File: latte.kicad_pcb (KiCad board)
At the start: 4 copper layers, 50 x 50 mm, 76 parts, among them J1 SOIC bite, J2 USB_C_Receptacle_USB2.0, J3 USB_C_Receptacle_USB2.0, J4 USB_C_2.0, J5 USB_A, J6 OUT1, J8 SENSE1, Q1 IRLML0030, SW1 USB BOOT, U1 RP2040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

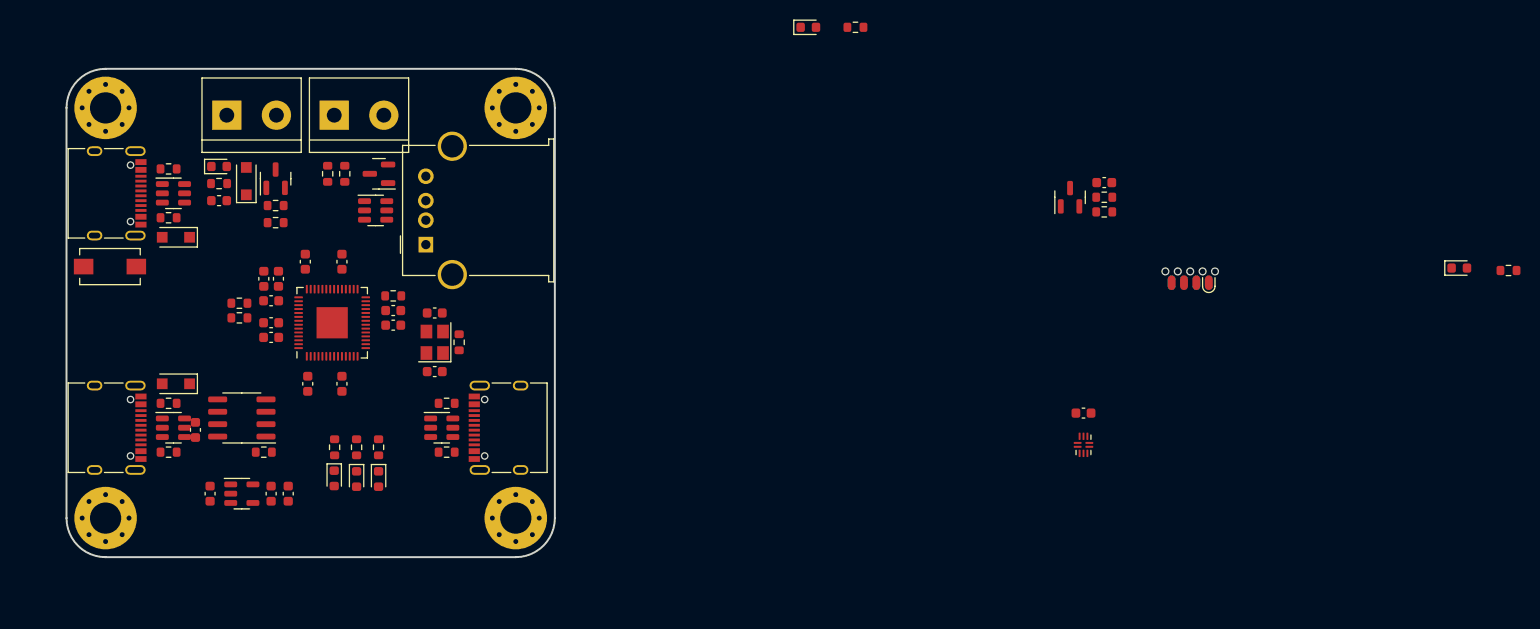
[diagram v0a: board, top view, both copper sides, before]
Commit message: Diff pair routing done
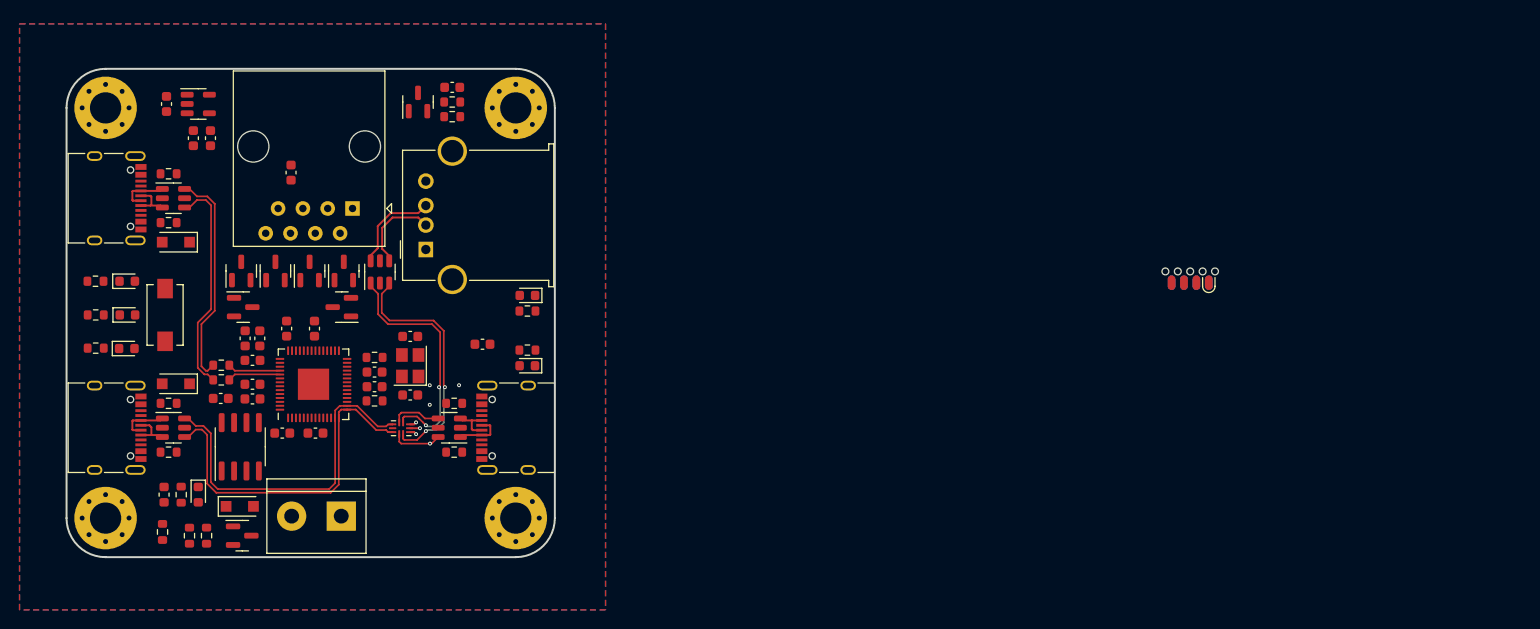
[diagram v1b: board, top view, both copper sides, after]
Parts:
- removed D13: BAV99, Package_TO_SOT_SMD:SOT-23
- removed J8: SENSE1, TerminalBlock:TerminalBlock_bornier-2_P5.08mm
- removed R27: 10k, Resistor_SMD:R_0603_1608Metric
- removed R29: DNP, Resistor_SMD:R_0603_1608Metric
- added C20: 100n, Capacitor_SMD:C_0603_1608Metric, F.Cu at (135.2, 81.6)
- added D11: BAV99, Package_TO_SOT_SMD:SOT-23, F.Cu at (133.6, 91.7)
- added D12: BAV99, Package_TO_SOT_SMD:SOT-23, F.Cu at (130.1, 91.7)
- added D15: BAV99, Package_TO_SOT_SMD:SOT-23, F.Cu at (137.1, 91.7)
- added D16: BAV99, Package_TO_SOT_SMD:SOT-23, F.Cu at (140.4, 95.4)
- added D17: BAV99, Package_TO_SOT_SMD:SOT-23, F.Cu at (140.6, 91.7)
- added D4: BAV99, Package_TO_SOT_SMD:SOT-23, F.Cu at (130.3, 95.4)
- added J7: SMART PROBE, Connector_RJ:RJ45_Amphenol_54602-x08_Horizontal, F.Cu at (141.5, 85.3)
- moved R16 100.8 mm to (159.4, 99.8), turned to 180 degrees
- moved D6 95.9 mm to (159.4, 101.4), turned to 180 degrees
- moved U6 69.9 mm to (146.5, 107.8), turned to -90 degrees
- moved C19 67.5 mm to (151.7, 72.9)
- moved D3 67.5 mm to (148.2, 74.4)
- moved R30 67.5 mm to (151.7, 75.9)
- moved R31 67.5 mm to (151.7, 74.4)
- moved C18 61.9 mm to (154.8, 99.2)
- moved R15 44.4 mm to (159.4, 95.8)
- moved J6 42.7 mm to (140.3, 116.8), turned to 180 degrees
- moved C1 40.1 mm to (122.5, 74.6)
- moved U3 40.1 mm to (125.7, 74.6)
- moved D5 39.8 mm to (159.4, 94.2), turned to 180 degrees
- moved C3 37.7 mm to (125.2, 78.1), turned to 90 degrees
- moved C2 36.9 mm to (127.0, 78.1), turned to 90 degrees
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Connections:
- net Net-(J5-Pad2) renamed /USBA_D-
- net Net-(J5-Pad3) renamed /USBA_D+
- net Net-(U1-Pad46) renamed /D-
- net Net-(U1-Pad47) renamed /D+
- net Net-(U6-Pad1) renamed /DUT_USBA_D+
- net Net-(U6-Pad7) renamed /DUT_USBA_D-
- net Net-(U7-Pad4) renamed /DUT_USBC_D+
- net Net-(U7-Pad6) renamed /DUT_USBC_D-
- U1 pad 15: unconnected-(U1-Pad15) -> /DUT_USB_D-
- U1 pad 16: unconnected-(U1-Pad16) -> /DUT_USB_D+
- U1 pad 4: unconnected-(U1-Pad4) -> /SMART_SDA
- U1 pad 5: unconnected-(U1-Pad5) -> /SMART_SCL
- U1 pad 6: unconnected-(U1-Pad6) -> /SMART_MISC1
- U1 pad 7: unconnected-(U1-Pad7) -> /SMART_MISC2
- U1 pad 8: unconnected-(U1-Pad8) -> /SMART_MISC3
- U1 pad 9: unconnected-(U1-Pad9) -> /SMART_SENSE
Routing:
- net /DUT_USB_D+: track 0.00 -> 36.1 mm
- net /DUT_USB_D-: track 0.00 -> 36.1 mm
- net /DUT_USBA_D-: track 0.00 -> 25.4 mm, vias 0 -> 2
- net /DUT_USBA_D+: track 0.00 -> 24.8 mm, vias 0 -> 2
- net /USB_D-: track 0.00 -> 22.6 mm
- net /USB_D+: track 0.00 -> 22.6 mm
- net /USBA_D+: track 0.00 -> 9.65 mm
- net /USBA_D-: track 0.00 -> 8.91 mm
- net /D-: track 0.00 -> 5.25 mm
- net /D+: track 0.00 -> 5.25 mm
- net /DUT_USBC_D-: track 0.00 -> 5.12 mm, vias 0 -> 1
- net /DUT_USBC_D+: track 0.00 -> 5.10 mm
- net Net-(J2-PadA7): track 0.00 -> 4.97 mm
- net Net-(J4-PadA7): track 0.00 -> 4.97 mm
- net Net-(J3-PadA7): track 0.00 -> 4.97 mm
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- added copper zone on B.Cu, net GND
- added copper zone on F.Cu, net GND
- added copper zone on In1.Cu, net GND
- added copper zone on In2.Cu, net GND

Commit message: Routing done
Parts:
- removed C20: 100n, Capacitor_SMD:C_0603_1608Metric
- moved J1 82.8 mm to (149.0, 120.6)
- moved R5 27.3 mm to (122.7, 91.1), turned to 0 degrees
- moved R24 19.5 mm to (143.4, 116.1)
- moved D10 18.3 mm to (143.4, 119.2), turned to 90 degrees
- moved C18 14.4 mm to (146.0, 110.6)
- moved F1 3.75 mm to (121.6, 118.3)
- moved R20 3.39 mm to (123.2, 118.3)
- moved D9 3.28 mm to (115.2, 92.1), turned to 180 degrees
- moved R19 3.27 mm to (118.4, 92.1), turned to 0 degrees
- moved D8 3.26 mm to (115.2, 96.0), turned to 180 degrees
- moved R17 3.19 mm to (118.4, 99.9), turned to 0 degrees
- moved D7 3.19 mm to (115.2, 99.9), turned to 180 degrees
- moved R18 3.19 mm to (118.4, 96.0), turned to 0 degrees
- moved Q1 2.86 mm to (127.4, 118.2), turned to 90 degrees
- moved D14 2.46 mm to (130.5, 118.2), turned to 90 degrees
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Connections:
- D7 pad 2: Net-(D7-Pad2) -> Net-(U1-Pad31)
- D9 pad 2: Net-(D9-Pad2) -> Net-(U1-Pad29)
- U1 pad 17: Net-(D7-Pad2) -> unconnected-(U1-Pad17)
- U1 pad 18: Net-(D8-Pad2) -> unconnected-(U1-Pad18)
- U1 pad 27: Net-(D9-Pad2) -> unconnected-(U1-Pad27)
- U1 pad 29: unconnected-(U1-Pad29) -> Net-(U1-Pad29)
- U1 pad 3: /OUT2 -> unconnected-(U1-Pad3)
- U1 pad 30: unconnected-(U1-Pad30) -> Net-(D8-Pad2)
- U1 pad 31: unconnected-(U1-Pad31) -> Net-(U1-Pad31)
- U1 pad 38: /SENSE1 -> unconnected-(U1-Pad38)
- U1 pad 39: /SENSE2 -> /SMART_SENSE
- U1 pad 9: /SMART_SENSE -> unconnected-(U1-Pad9)
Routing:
- net +3V3: track 1.05 -> 72.3 mm, vias 1 -> 26
- net Net-(U1-Pad31): track 0.00 -> 67.7 mm, vias 0 -> 2
- net Net-(D8-Pad2): track 0.00 -> 65.5 mm, vias 0 -> 2
- net Net-(U1-Pad29): track 0.00 -> 65.4 mm, vias 0 -> 2
- net /SMART_MISC2: track 0.00 -> 53.3 mm, vias 0 -> 2
- net /VBUS_SENSE: track 0.00 -> 45.0 mm, vias 0 -> 2
- net +5V: track 0.00 -> 44.7 mm, vias 0 -> 15
- net /SMART_MISC3: track 0.00 -> 41.5 mm, vias 0 -> 2
- net Net-(R5-Pad2): track 0.00 -> 39.2 mm, vias 0 -> 2
- net /DUT_USB_S: track 0.73 -> 39.2 mm, vias 1 -> 3
- net /~{RST}: track 0.00 -> 32.9 mm, vias 0 -> 2
- net /SMART_MISC1: track 0.00 -> 32.3 mm, vias 0 -> 2
- net VBUS: track 0.00 -> 32.3 mm, vias 0 -> 18
- net /SMART_SCL: track 0.00 -> 28.1 mm, vias 0 -> 2
- net /OUT1: track 0.00 -> 27.9 mm, vias 0 -> 2
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- added copper zone on In2.Cu, net +3V3
- added copper zone on In2.Cu, net +5V
- added copper zone on In2.Cu, net Net-(D1-Pad2)
- added copper zone on In2.Cu, net VBUS
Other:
- board text added: "ACTUATOR"
- board text added: "DUT A"
- board text added: "DUT C"
- board text added: "LATTE 1.0 Vojtěch Vosáhlo 13.11.2022"
- board text added: "PC COMM"
- board text added: "PC DUT"
- board text added: "SENSOR"
- board text added: "SWD"
- board text added: "USB BOOT"
- board text added: "{ "ViaStitching": "0.1", "stitch_zone_0": { "HSpacing": "3", "VSpacing": "3", "Clearance": "0", "Randomize": false }, "stitch_zone_1": { "HSpacing": "3", "VSpacing": "3", "Clearance": "1", "Randomize": false } }"

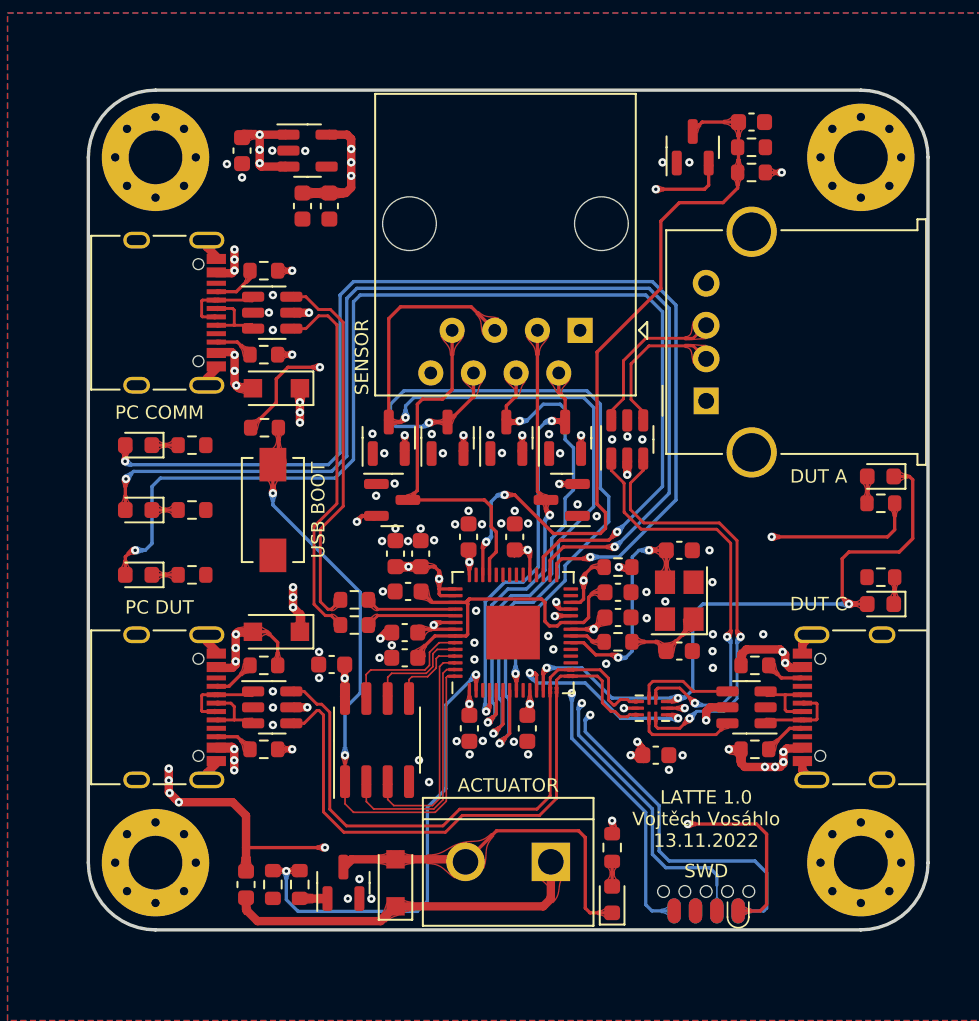
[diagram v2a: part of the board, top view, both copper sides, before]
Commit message: Added via stitching
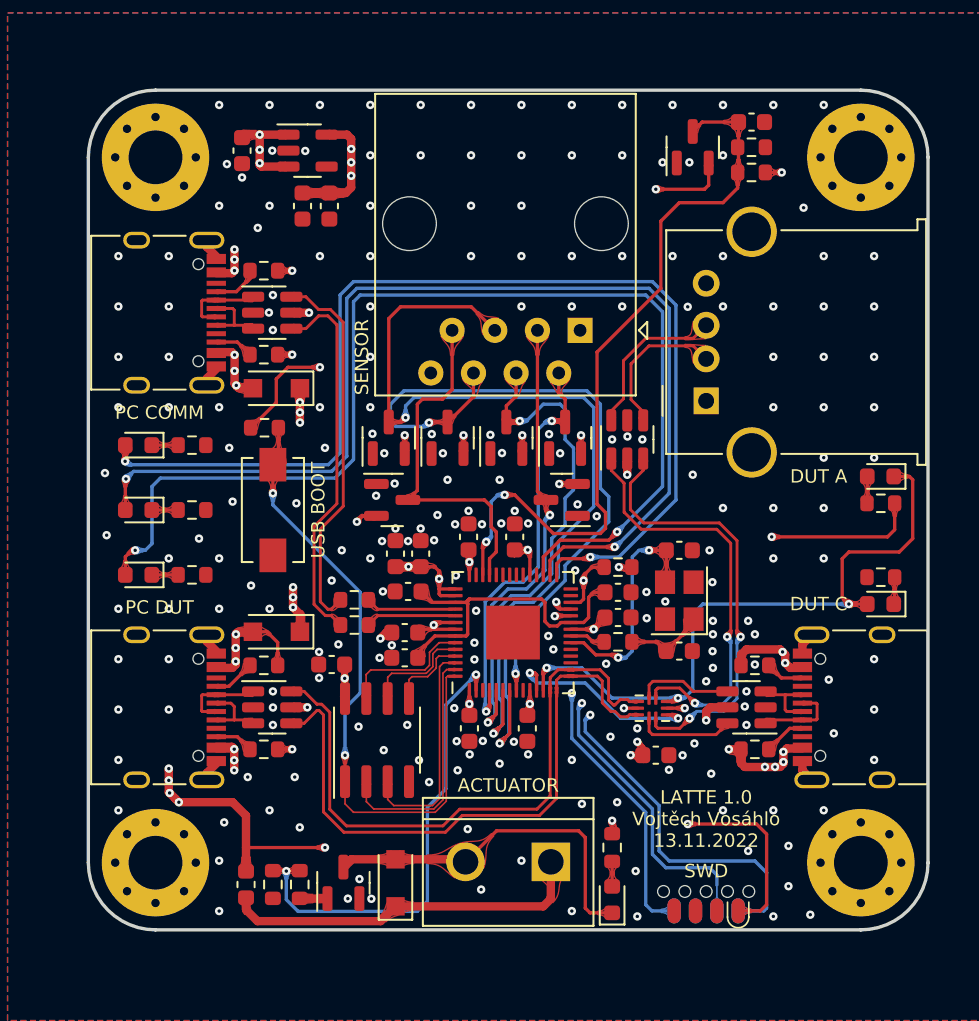
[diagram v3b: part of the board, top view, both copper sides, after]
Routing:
- net GND: vias 72 -> 219
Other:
- board text added: "{ "ViaStitching": "0.1", "stitch_zone_0": { "HSpacing": "3", "VSpacing": "3", "Clearance": "0", "Randomize": false }, "stitch_zone_1": { "HSpacing": "1", "VSpacing": "1", "Clearance": "0", "Randomize": false } }"
- board text removed: "{ "ViaStitching": "0.1", "stitch_zone_0": { "HSpacing": "3", "VSpacing": "3", "Clearance": "0", "Randomize": false }, "stitch_zone_1": { "HSpacing": "3", "VSpacing": "3", "Clearance": "1", "Randomize": false } }"

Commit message: Added logo
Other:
- board text added: "JLCJLCJLCJLC"
- board text added: "LATTE 1.0 13.11.2022"
- board text added: "Vojtěch Vosáhlo"
- board text removed: "LATTE 1.0 Vojtěch Vosáhlo 13.11.2022"

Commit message: Finalized for production
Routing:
- net /DUT_USBA_D+: track 25.5 -> 26.1 mm
- net /DUT_USB_D+: track 37.1 -> 37.8 mm
- net GND: vias 219 -> 217
